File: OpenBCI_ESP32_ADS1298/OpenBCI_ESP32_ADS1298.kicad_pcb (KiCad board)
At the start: 6 copper layers, 50 x 50 mm, 75 parts, among them J1 Conn_02x13_Odd_Even, J2 Conn_02x08_Odd_Even, J3 Conn_02x03_Odd_Even, J4 Conn_02x02_Odd_Even, J5 Conn_01x02, J6 Conn_01x02, J7 Conn_01x02, U1 TPD4E1B06, U2 TPD4E1B06, U3 TPD4E1B06, U4 TPD4E1B06, U5 TPD4E1B06, U6 TPD4E1B06, U7 ADS1298RIZXGR

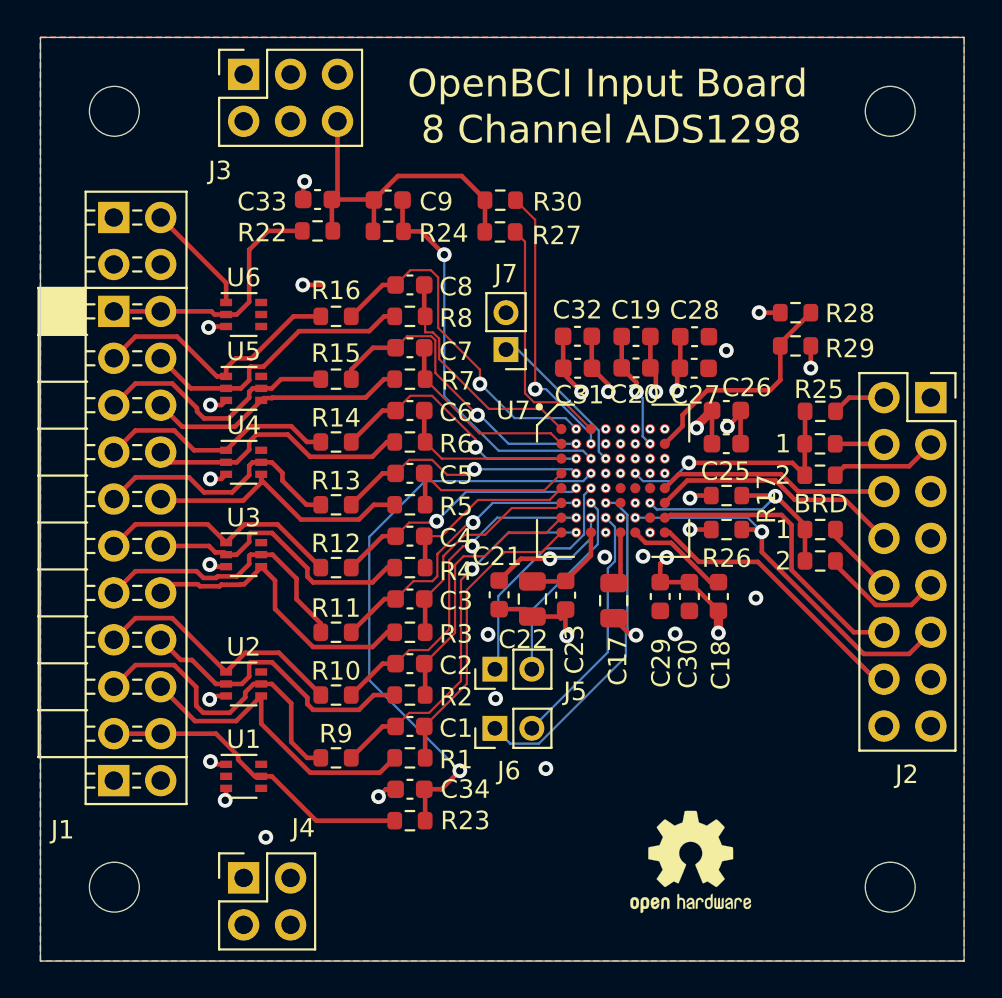
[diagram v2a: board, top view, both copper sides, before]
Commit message: Fix ADS1298 Mounting Holes
Fix ADS1298R Mounting holes shorting layers
Add some ADS1298R Arduino Files
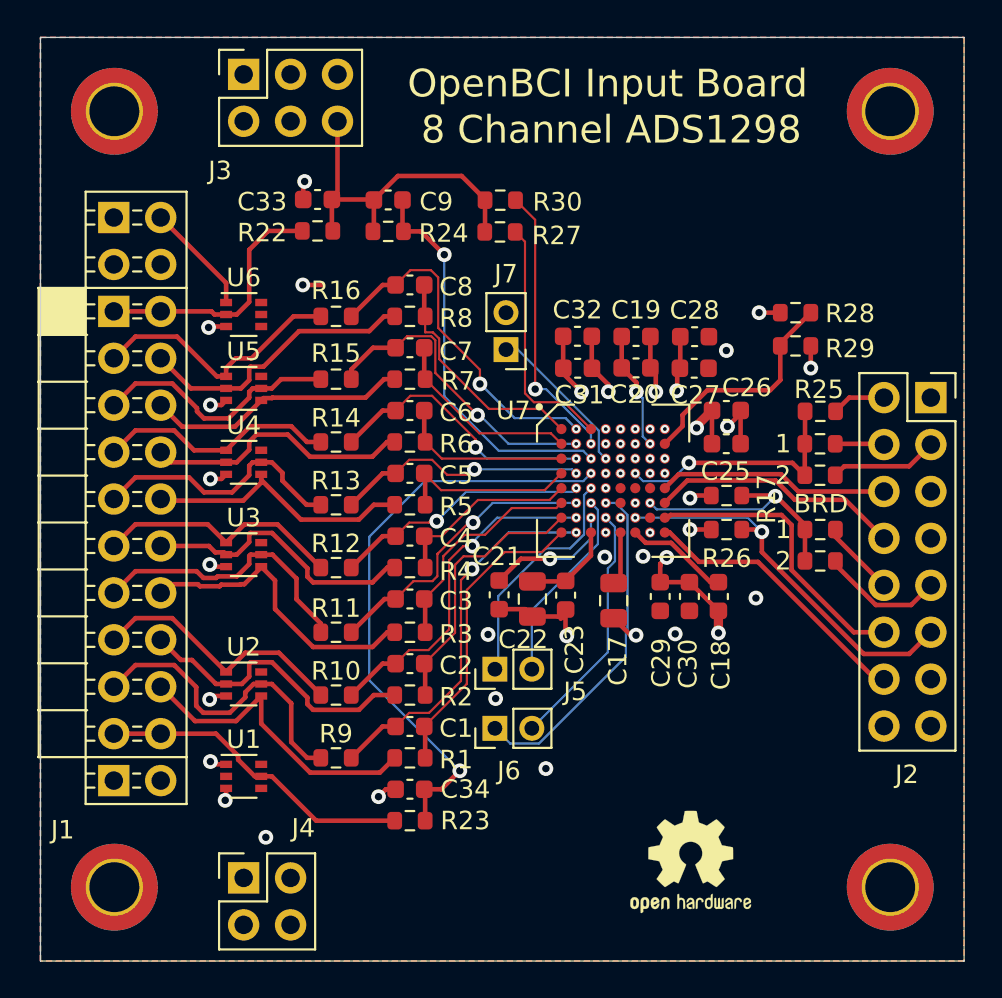
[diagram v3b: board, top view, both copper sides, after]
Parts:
- H1, H2, H3, H4: footprint MountingHole:MountingHole_2.7mm_M2.5 -> MountingHole:MountingHole_2.7mm_M2.5_DIN965_Pad_TopBottom
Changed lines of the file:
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@@
     )
   )
-  (footprint "MountingHole:MountingHole_2.7mm_M2.5" (layer "F.Cu")
+  (footprint "MountingHole:MountingHole_2.7mm_M2.5_DIN965_Pad_TopBottom" (layer "F.Cu")
     (at 104 54)
-    (descr "Mounting Hole 2.7mm, no annular, M2.5")
-    (tags "mounting hole 2.7mm no annular m2.5")
+    (descr "Mounting Hole 2.7mm, M2.5, DIN965")
+    (tags "mounting hole 2.7mm m2.5 din965")
     (property "Sheetfile" "Analog_Input.kicad_sch")
     (property "Sheetname" "Analog_Input")
-    (property "ki_description" "Mounting Hole without connection")
+    (property "ki_description" "Mounting Hole with connection")
     (property "ki_keywords" "mounting hole")
     (attr exclude_from_pos_files)
-    (fp_text reference "H1" (at 0 -3.7) (layer "F.SilkS") hide
+    (fp_text reference "H1" (at 0 -3.35) (layer "F.SilkS") hide
         (effects (font (size 1 1) (thickness 0.15)))
     )
-    (fp_text value "MountingHole" (at 0 3.7) (layer "F.Fab")
+    (fp_text value "MountingHole" (at 0 3.35) (layer "F.Fab")
         (effects (font (size 1 1) (thickness 0.15)))
     )
@@
         (effects (font (size 1 1) (thickness 0.15)))
     )
-    (fp_circle (center 0 0) (end 2.7 0)
+    (fp_circle (center 0 0) (end 2.35 0)
       (stroke (width 0.15) (type solid)) (fill none) (layer "Cmts.User"))
-    (fp_circle (center 0 0) (end 2.95 0)
+    (fp_circle (center 0 0) (end 2.6 0)
       (stroke (width 0.05) (type solid)) (fill none) (layer "F.CrtYd"))
-    (pad "" np_thru_hole circle (at 0 0) (size 2.7 2.7) (drill 2.7) (layers "*.Cu" "*.Mask"))
+    (pad "1" thru_hole circle (at 0 0) (size 3.1 3.1) (drill 2.7) (layers "*.Cu" "*.Mask")
+      (net 1 "GND") (pinfunction "1") (pintype "input"))
+    (pad "1" connect circle (at 0 0) (size 4.7 4.7) (layers "F.Cu" "F.Mask")
+      (net 1 "GND") (pinfunction "1") (pintype "input"))
+    (pad "1" connect circle (at 0 0) (size 4.7 4.7) (layers "B.Cu" "B.Mask")
+      (net 1 "GND") (pinfunction "1") (pintype "input"))
   )
-  (footprint "MountingHole:MountingHole_2.7mm_M2.5" (layer "F.Cu")
+  (footprint "MountingHole:MountingHole_2.7mm_M2.5_DIN965_Pad_TopBottom" (layer "F.Cu")
     (at 104 96)
-    (descr "Mounting Hole 2.7mm, no annular, M2.5")
-    (tags "mounting hole 2.7mm no annular m2.5")
+    (descr "Mounting Hole 2.7mm, M2.5, DIN965")
+    (tags "mounting hole 2.7mm m2.5 din965")
     (property "Sheetfile" "Analog_Input.kicad_sch")
     (property "Sheetname" "Analog_Input")
-    (property "ki_description" "Mounting Hole without connection")
+    (property "ki_description" "Mounting Hole with connection")
     (property "ki_keywords" "mounting hole")
     (attr exclude_from_pos_files)
-    (fp_text reference "H2" (at 0 -3.7) (layer "F.SilkS") hide
+    (fp_text reference "H2" (at 0 -3.35) (layer "F.SilkS") hide
         (effects (font (size 1 1) (thickness 0.15)))
     )
-    (fp_text value "MountingHole" (at 0 3.7) (layer "F.Fab")
+    (fp_text value "MountingHole" (at 0 3.35) (layer "F.Fab")
         (effects (font (size 1 1) (thickness 0.15)))
     )
@@
         (effects (font (size 1 1) (thickness 0.15)))
     )
-    (fp_circle (center 0 0) (end 2.7 0)
+    (fp_circle (center 0 0) (end 2.35 0)
       (stroke (width 0.15) (type solid)) (fill none) (layer "Cmts.User"))
-    (fp_circle (center 0 0) (end 2.95 0)
+    (fp_circle (center 0 0) (end 2.6 0)
       (stroke (width 0.05) (type solid)) (fill none) (layer "F.CrtYd"))
-    (pad "" np_thru_hole circle (at 0 0) (size 2.7 2.7) (drill 2.7) (layers "*.Cu" "*.Mask"))
+    (pad "1" thru_hole circle (at 0 0) (size 3.1 3.1) (drill 2.7) (layers "*.Cu" "*.Mask")
+      (net 1 "GND") (pinfunction "1") (pintype "input"))
+    (pad "1" connect circle (at 0 0) (size 4.7 4.7) (layers "F.Cu" "F.Mask")
+      (net 1 "GND") (pinfunction "1") (pintype "input"))
+    (pad "1" connect circle (at 0 0) (size 4.7 4.7) (layers "B.Cu" "B.Mask")
+      (net 1 "GND") (pinfunction "1") (pintype "input"))
   )
-  (footprint "MountingHole:MountingHole_2.7mm_M2.5" (layer "F.Cu")
+  (footprint "MountingHole:MountingHole_2.7mm_M2.5_DIN965_Pad_TopBottom" (layer "F.Cu")
     (at 146 54)
-    (descr "Mounting Hole 2.7mm, no annular, M2.5")
-    (tags "mounting hole 2.7mm no annular m2.5")
+    (descr "Mounting Hole 2.7mm, M2.5, DIN965")
+    (tags "mounting hole 2.7mm m2.5 din965")
     (property "Sheetfile" "Analog_Input.kicad_sch")
     (property "Sheetname" "Analog_Input")
-    (property "ki_description" "Mounting Hole without connection")
+    (property "ki_description" "Mounting Hole with connection")
     (property "ki_keywords" "mounting hole")
     (attr exclude_from_pos_files)
-    (fp_text reference "H3" (at 0 -3.7) (layer "F.SilkS") hide
+    (fp_text reference "H3" (at 0 -3.35) (layer "F.SilkS") hide
         (effects (font (size 1 1) (thickness 0.15)))
     )
-    (fp_text value "MountingHole" (at 0 3.7) (layer "F.Fab")
+    (fp_text value "MountingHole" (at 0 3.35) (layer "F.Fab")
         (effects (font (size 1 1) (thickness 0.15)))
     )
@@
         (effects (font (size 1 1) (thickness 0.15)))
     )
-    (fp_circle (center 0 0) (end 2.7 0)
+    (fp_circle (center 0 0) (end 2.35 0)
       (stroke (width 0.15) (type solid)) (fill none) (layer "Cmts.User"))
-    (fp_circle (center 0 0) (end 2.95 0)
+    (fp_circle (center 0 0) (end 2.6 0)
       (stroke (width 0.05) (type solid)) (fill none) (layer "F.CrtYd"))
-    (pad "" np_thru_hole circle (at 0 0) (size 2.7 2.7) (drill 2.7) (layers "*.Cu" "*.Mask"))
+    (pad "1" thru_hole circle (at 0 0) (size 3.1 3.1) (drill 2.7) (layers "*.Cu" "*.Mask")
+      (net 1 "GND") (pinfunction "1") (pintype "input"))
+    (pad "1" connect circle (at 0 0) (size 4.7 4.7) (layers "F.Cu" "F.Mask")
+      (net 1 "GND") (pinfunction "1") (pintype "input"))
+    (pad "1" connect circle (at 0 0) (size 4.7 4.7) (layers "B.Cu" "B.Mask")
+      (net 1 "GND") (pinfunction "1") (pintype "input"))
   )
-  (footprint "MountingHole:MountingHole_2.7mm_M2.5" (layer "F.Cu")
+  (footprint "MountingHole:MountingHole_2.7mm_M2.5_DIN965_Pad_TopBottom" (layer "F.Cu")
     (at 146 96)
-    (descr "Mounting Hole 2.7mm, no annular, M2.5")
-    (tags "mounting hole 2.7mm no annular m2.5")
+    (descr "Mounting Hole 2.7mm, M2.5, DIN965")
+    (tags "mounting hole 2.7mm m2.5 din965")
     (property "Sheetfile" "Analog_Input.kicad_sch")
     (property "Sheetname" "Analog_Input")
-    (property "ki_description" "Mounting Hole without connection")
+    (property "ki_description" "Mounting Hole with connection")
     (property "ki_keywords" "mounting hole")
     (attr exclude_from_pos_files)
-    (fp_text reference "H4" (at 0 -3.7) (layer "F.SilkS") hide
+    (fp_text reference "H4" (at 0 -3.35) (layer "F.SilkS") hide
         (effects (font (size 1 1) (thickness 0.15)))
     )
-    (fp_text value "MountingHole" (at 0 3.7) (layer "F.Fab")
+    (fp_text value "MountingHole" (at 0 3.35) (layer "F.Fab")
         (effects (font (size 1 1) (thickness 0.15)))
     )
@@
         (effects (font (size 1 1) (thickness 0.15)))
     )
-    (fp_circle (center 0 0) (end 2.7 0)
+    (fp_circle (center 0 0) (end 2.35 0)
       (stroke (width 0.15) (type solid)) (fill none) (layer "Cmts.User"))
-    (fp_circle (center 0 0) (end 2.95 0)
+    (fp_circle (center 0 0) (end 2.6 0)
       (stroke (width 0.05) (type solid)) (fill none) (layer "F.CrtYd"))
-    (pad "" np_thru_hole circle (at 0 0) (size 2.7 2.7) (drill 2.7) (layers "*.Cu" "*.Mask"))
+    (pad "1" thru_hole circle (at 0 0) (size 3.1 3.1) (drill 2.7) (layers "*.Cu" "*.Mask")
+      (net 1 "GND") (pinfunction "1") (pintype "input"))
+    (pad "1" connect circle (at 0 0) (size 4.7 4.7) (layers "F.Cu" "F.Mask")
+      (net 1 "GND") (pinfunction "1") (pintype "input"))
+    (pad "1" connect circle (at 0 0) (size 4.7 4.7) (layers "B.Cu" "B.Mask")
+      (net 1 "GND") (pinfunction "1") (pintype "input"))
   )
   (footprint "Symbol:OSHW-Logo2_7.3x6mm_SilkScreen" (layer "F.Cu")
